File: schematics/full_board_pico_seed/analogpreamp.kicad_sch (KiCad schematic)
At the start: 57 parts, among them J1 XLR3, J3 Aux In, J4 Conn_01x02_Pin, J7 XLR3, J8 XLR3, U4 OPA134, U7 OPA2342, U9 OPA4342

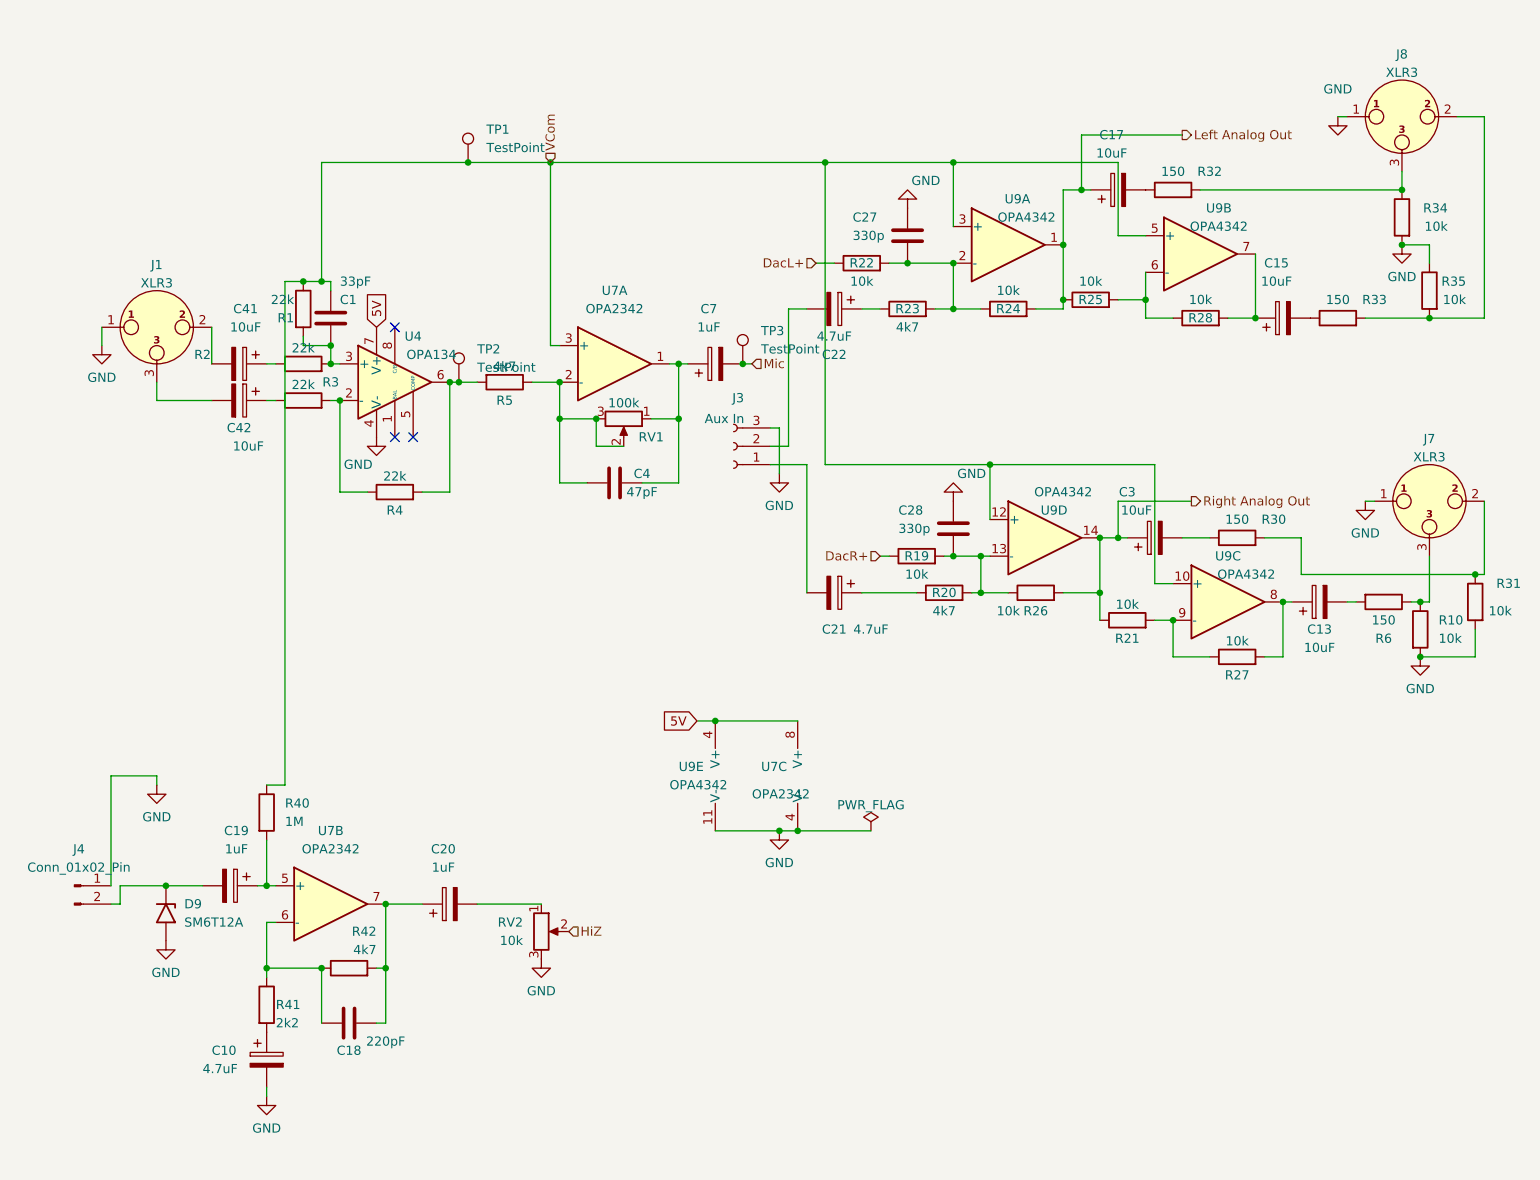
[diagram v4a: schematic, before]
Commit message: corrected schematic regarding pcm3060
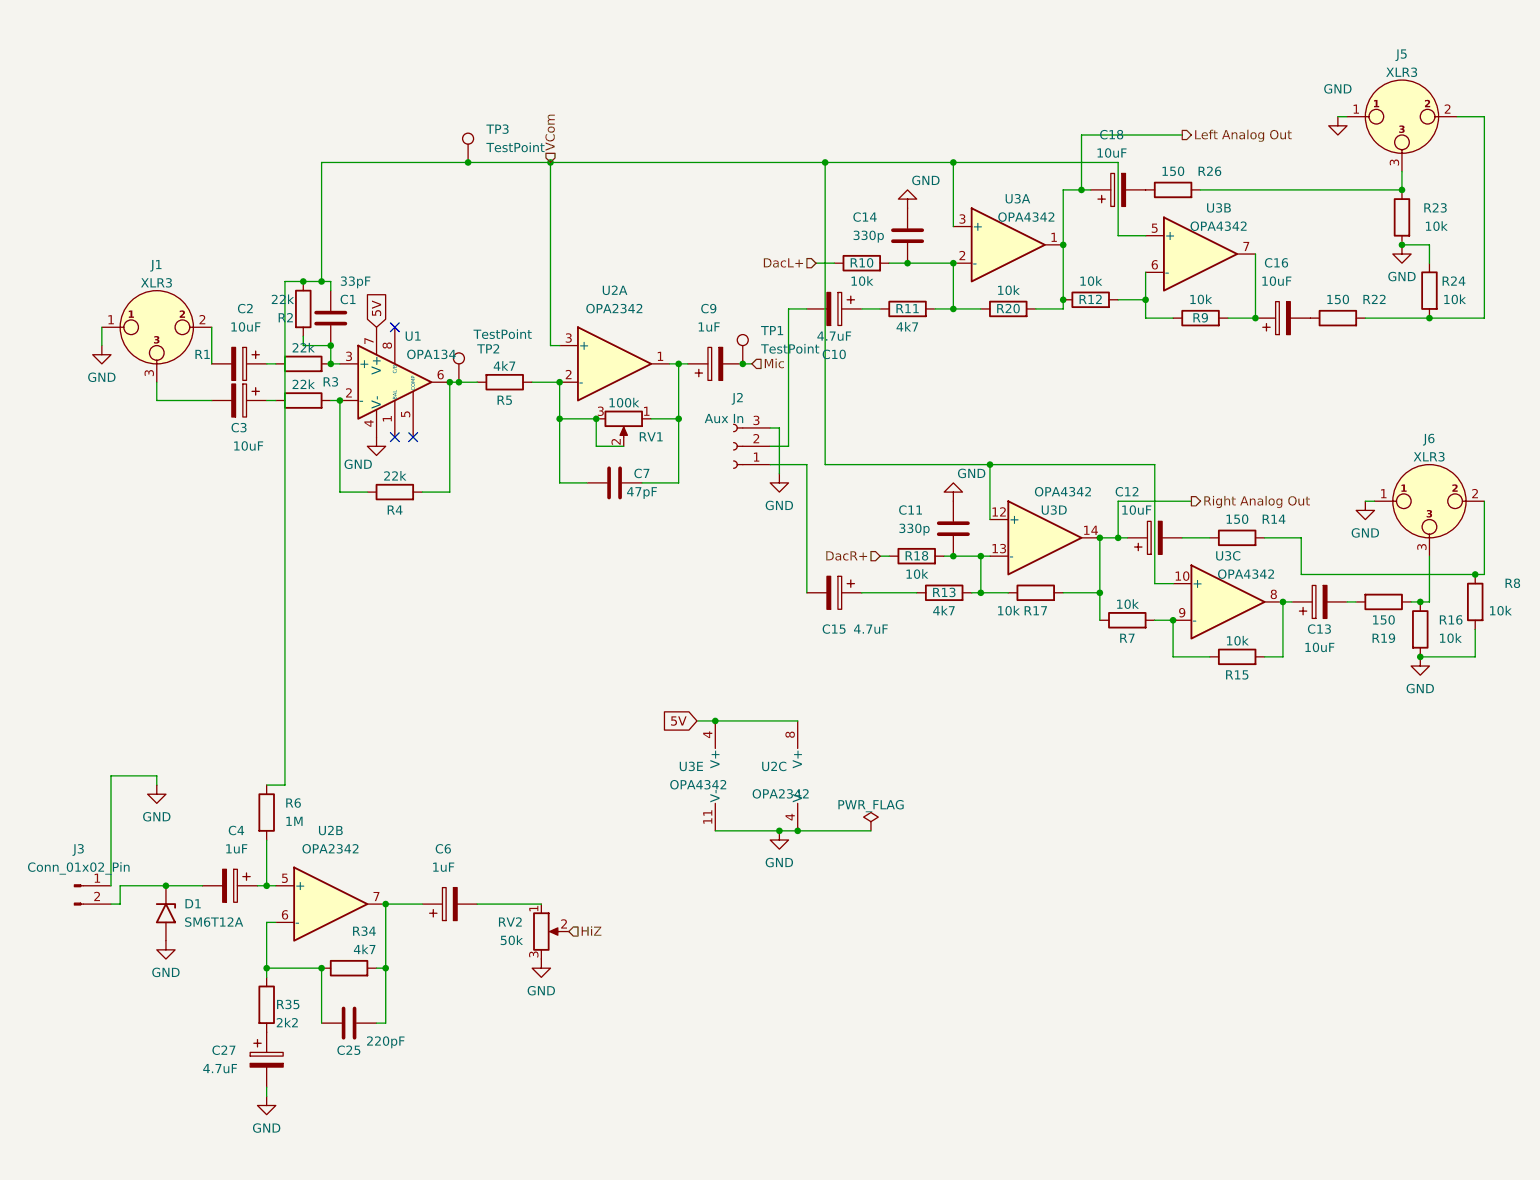
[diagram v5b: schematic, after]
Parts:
- RV2: value 10k -> 50k
- renumbered C22 to C10, C28 to C11, C3 to C12, C27 to C14, C21 to C15, C15 to C16, C17 to C18, C41 to C2, C18 to C25, C10 to C27, C42 to C3, C19 to C4, C20 to C6, C4 to C7, C7 to C9, D9 to D1, J3 to J2, J4 to J3, J8 to J5, J7 to J6, R2 to R1, R22 to R10, R23 to R11, R25 to R12, R20 to R13, R30 to R14, R27 to R15, R10 to R16, R26 to R17, R19 to R18, R6 to R19, R1 to R2, R24 to R20, R33 to R22, R34 to R23, R35 to R24, R32 to R26, R42 to R34, R41 to R35, R40 to R6, R21 to R7, R31 to R8, R28 to R9, TP3 to TP1, TP1 to TP3, U4 to U1, U7 to U2, U9 to U3

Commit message: schematic change
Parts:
- removed C12, C13, C16, C18: 10uF, Capacitor_SMD:CP_Elec_4x4.5, symbol Device:C_Polarized
- removed C6, C9: 1uF, Capacitor_SMD:CP_Elec_4x4.5, symbol Device:C_Polarized
- removed R16, R23, R24, R8: 10k, Resistor_SMD:R_0603_1608Metric_Pad0.98x0.95mm_HandSolder, symbol Device:R
- removed U1: OPA134, Package_SO:SOIC-8_3.9x4.9mm_P1.27mm, symbol Amplifier_Operational:NE5534
- added C11, C12, C14, C15: 4.7uF, Capacitor_SMD:CP_Elec_5x5.4, symbol Device:C
- added U1: OPA1602, Package_SO:SOIC-8_3.9x4.9mm_P1.27mm, symbol Amplifier_Operational:OPA1602
- renumbered C3 to C1, C15 to C10, C14 to C13, C27 to C22, C1 to C3, C7 to C4, C25 to C5, C4 to C6, C10 to C8, C11 to C9, J3 to J2, J6 to J3, J2 to J4, J5 to J6, R4 to R1, R7 to R10, R17 to R11, R11 to R12, R12 to R13, R9 to R14, R14 to R15, R15 to R16, R18 to R17, R20 to R18, R26 to R19, R5 to R2, R22 to R20, R2 to R29, R35 to R31, R1 to R4, R6 to R5, R34 to R6, R10 to R7, R19 to R8, R13 to R9, TP3 to TP1, TP1 to TP3
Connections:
- net 5V: now also U1.8 (V+)
- net GND: now also U1.4 (V-); no longer RV2.3
- net Left Analog Out: now also C15.1
- net Mic: now also C4.2, RV1.1, U2.1
- net Right Analog Out: now also C11.1
- net VCom: now also U1.5 (+); no longer C3.1, R29.1, R5.1, TP1.1, U2.3 (+), U3.10 (+), U3.12 (+), U3.3 (+), U3.5 (+)
- net at R16.2, U3.8: now also C12.1
- net at R1.1, R3.2: now also U1.2 (-)
- net at C3.2, R29.2, R4.2: now also U1.3 (+)
- net at R1.2, R2.2, TP2.1: now also U1.1
- net at R14.2, U3.7: now also C14.1
- net at R8.2: now also C12.2
- net at R19.1: now also C15.2
- net at RV2.1: now also C5.2, R6.2, U2.7
- net at R15.1: now also C11.2
- net at R20.1: now also C14.2
- new net: C3.1, R29.1, R5.1, RV2.3, TP1.1, U1.6 (-), U1.7, U2.3 (+), U3.10 (+), U3.12 (+), U3.3 (+), U3.5 (+)
- no-connect marks 3 -> 0

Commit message: updated schematic
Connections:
- net GND: now also J4.1 (Pin_1); no longer C13.1, C9.1, J4.3 (Pin_3)
- net Left Analog Out: now also C13.2
- net Right Analog Out: now also C9.2
- net at R11.1, R17.2, R9.2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: now also C9.1; no longer C9.2
- net at C10.2: now also J4.2 (Pin_2); no longer J4.1 (Pin_1)
- net at R12.2, R18.1, R7.2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: now also C13.1; no longer C13.2
- net at C8.2: now also J4.3 (Pin_3); no longer J4.2 (Pin_2)
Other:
- moved on the sheet: C13, C9
